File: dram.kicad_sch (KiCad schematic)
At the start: 29 parts

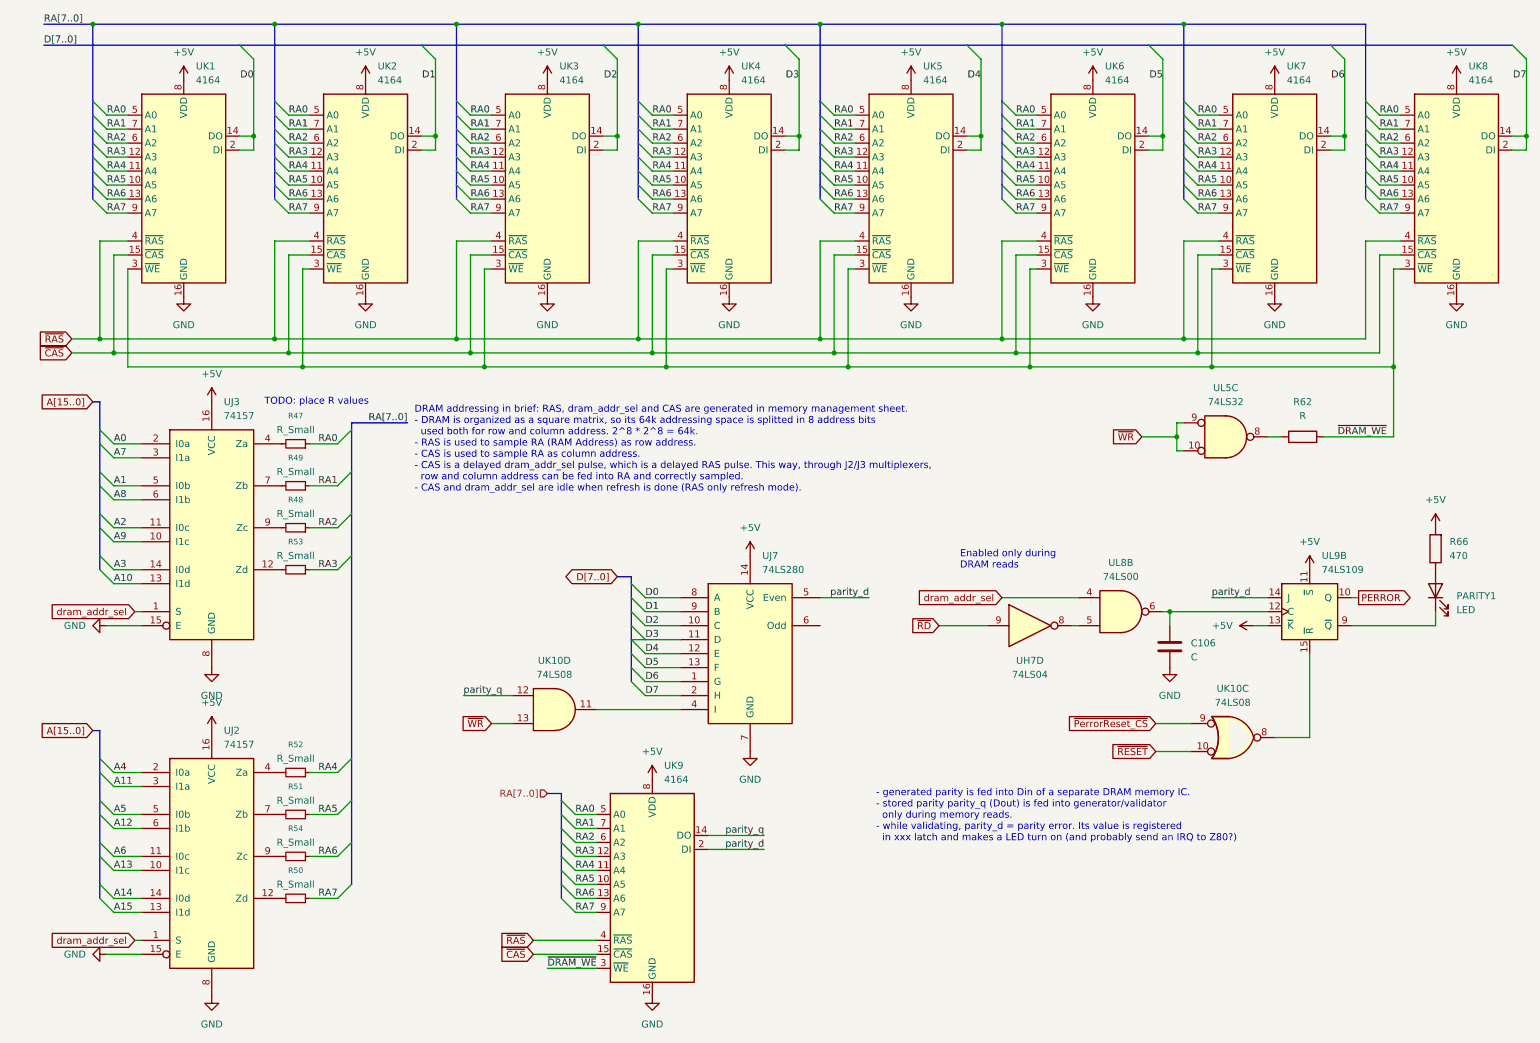
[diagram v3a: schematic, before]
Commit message: sch: added pin 1 to DRAM, pulled up
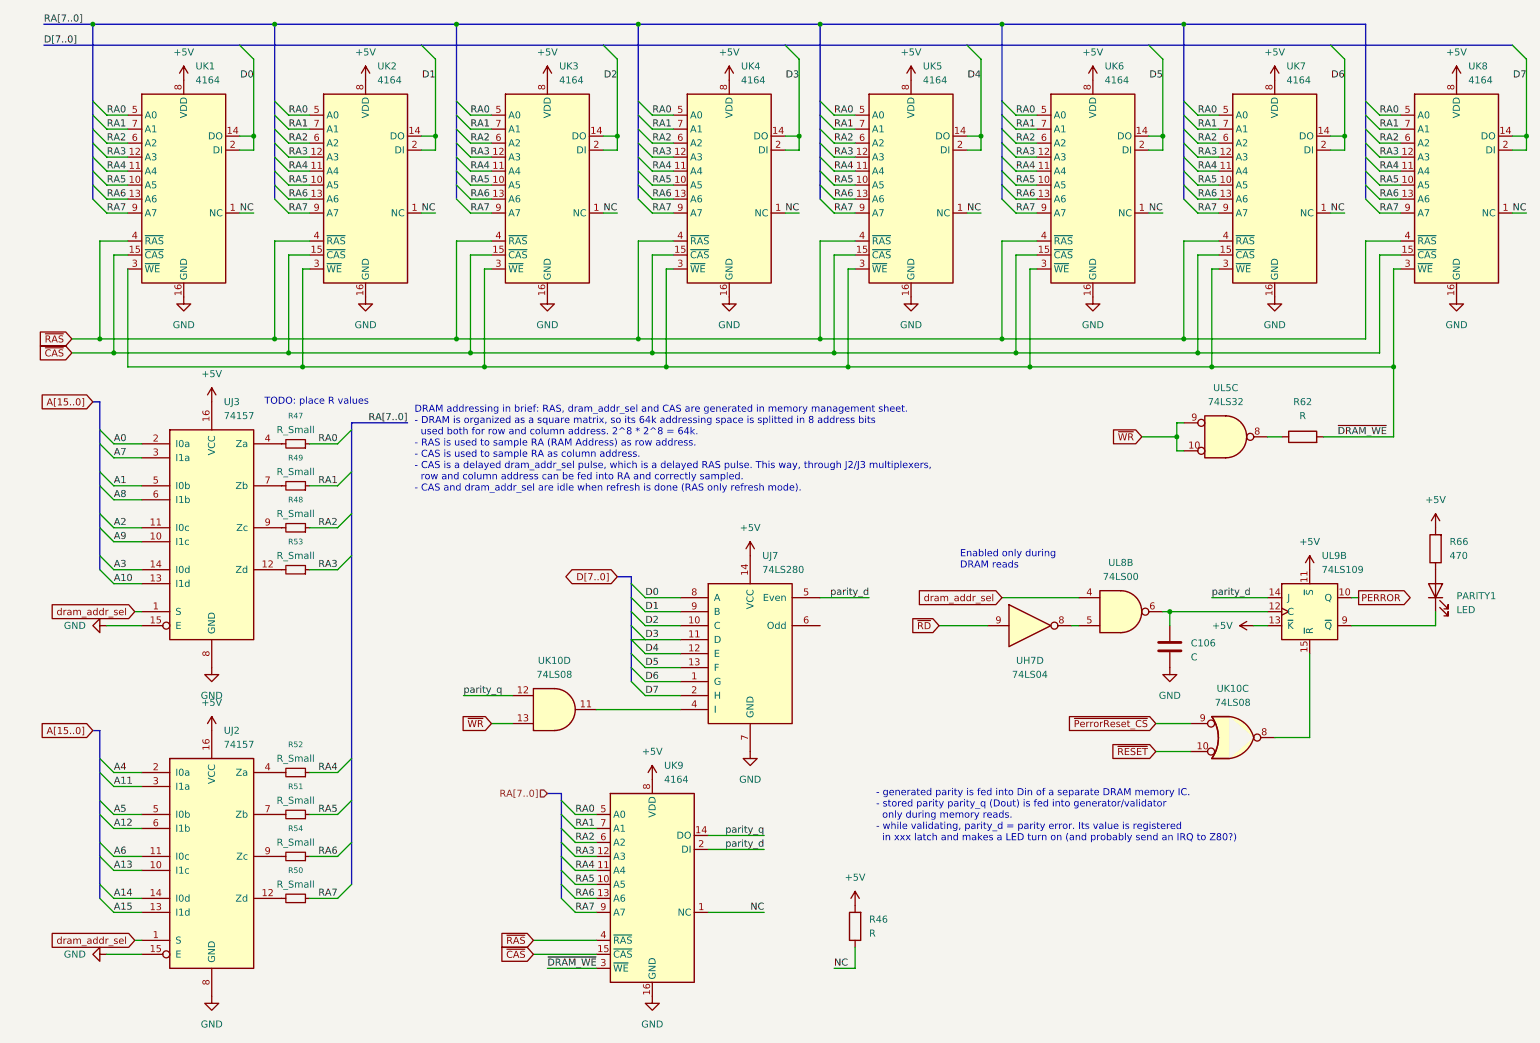
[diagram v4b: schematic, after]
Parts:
- added R46: R, Resistor_THT:R_Axial_DIN0204_L3.6mm_D1.6mm_P5.08mm_Vertical, symbol Device:R
- UK1, UK2, UK3, UK4, UK5, UK6, UK7, UK8, UK9: symbol Vintage:4164 -> ceda:4164
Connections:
- net +5V: now also R46.2
- net NC: now reaches UK9.1 (NC)
- net NC: now also UK1.1 (NC), UK2.1 (NC), UK3.1 (NC), UK4.1 (NC), UK5.1 (NC), UK6.1 (NC), UK7.1 (NC), UK8.1 (NC), R46.1
